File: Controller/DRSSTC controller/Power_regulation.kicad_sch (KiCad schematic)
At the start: 23 parts, among them J7 Conn_01x01_Female, J8 Screw_Terminal_01x02, J9 Conn_01x01_Female, U601 L7809, U602 L7805

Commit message: V0.2a
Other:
- company: (none) -> Politehnika
- title: (none) -> DRSSTC controller
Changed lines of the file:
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@@
 (kicad_sch (version 20211123) (generator eeschema)
   (paper "A4")
+  (title_block
+    (title "DRSSTC controller")
+    (date "2023-03-07")
+    (rev "0.2")
+    (company "Politehnika")
+  )
   (junction (at 122.555 86.995) (diameter 0) (color 0 0 0 0)
   )

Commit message: V0.2c
Added stl files
PCB update
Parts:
- C403: renamed from C602; footprint Capacitor_THT:CP_Radial_D5.0mm_P2.50mm -> Capacitor_THT:CP_Radial_D12.5mm_P5.00mm
- J404: renamed from J?; footprint (none) -> Connector_PinHeader_2.54mm:PinHeader_1x02_P2.54mm_Vertical
- U401: renamed from U?; footprint (none) -> Package_TO_SOT_SMD:TO-252-2
- gave numbers to parts that had none: 3
- renumbered C601 to C402, C603 to C406, C604 to C407, C605 to C408, C606 to C409, C607 to C410, D601 to D401, D602 to D402, D603 to D403, J7 to J401, J8 to J402, J9 to J403, R601 to R401, R602 to R402, R603 to R403, U601 to U402, U602 to U403

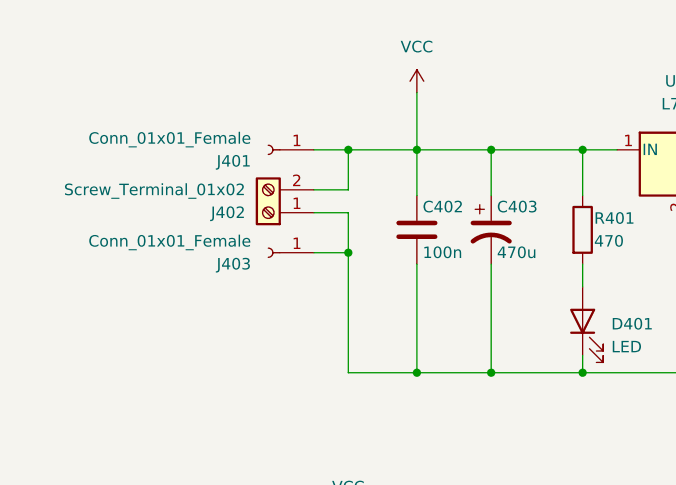
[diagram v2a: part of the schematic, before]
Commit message: Updated circuit
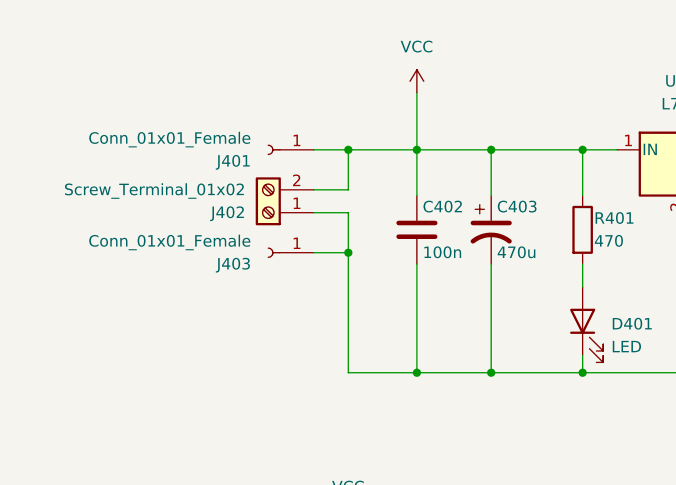
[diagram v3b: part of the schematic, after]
